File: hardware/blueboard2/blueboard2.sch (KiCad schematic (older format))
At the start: 142 parts, among them Q1 TRANSISTOR_NPN, Q2 TRANSISTOR_NPN, Q3 TRANSISTOR_NPN, SW2 SW_PUSHBUTTON

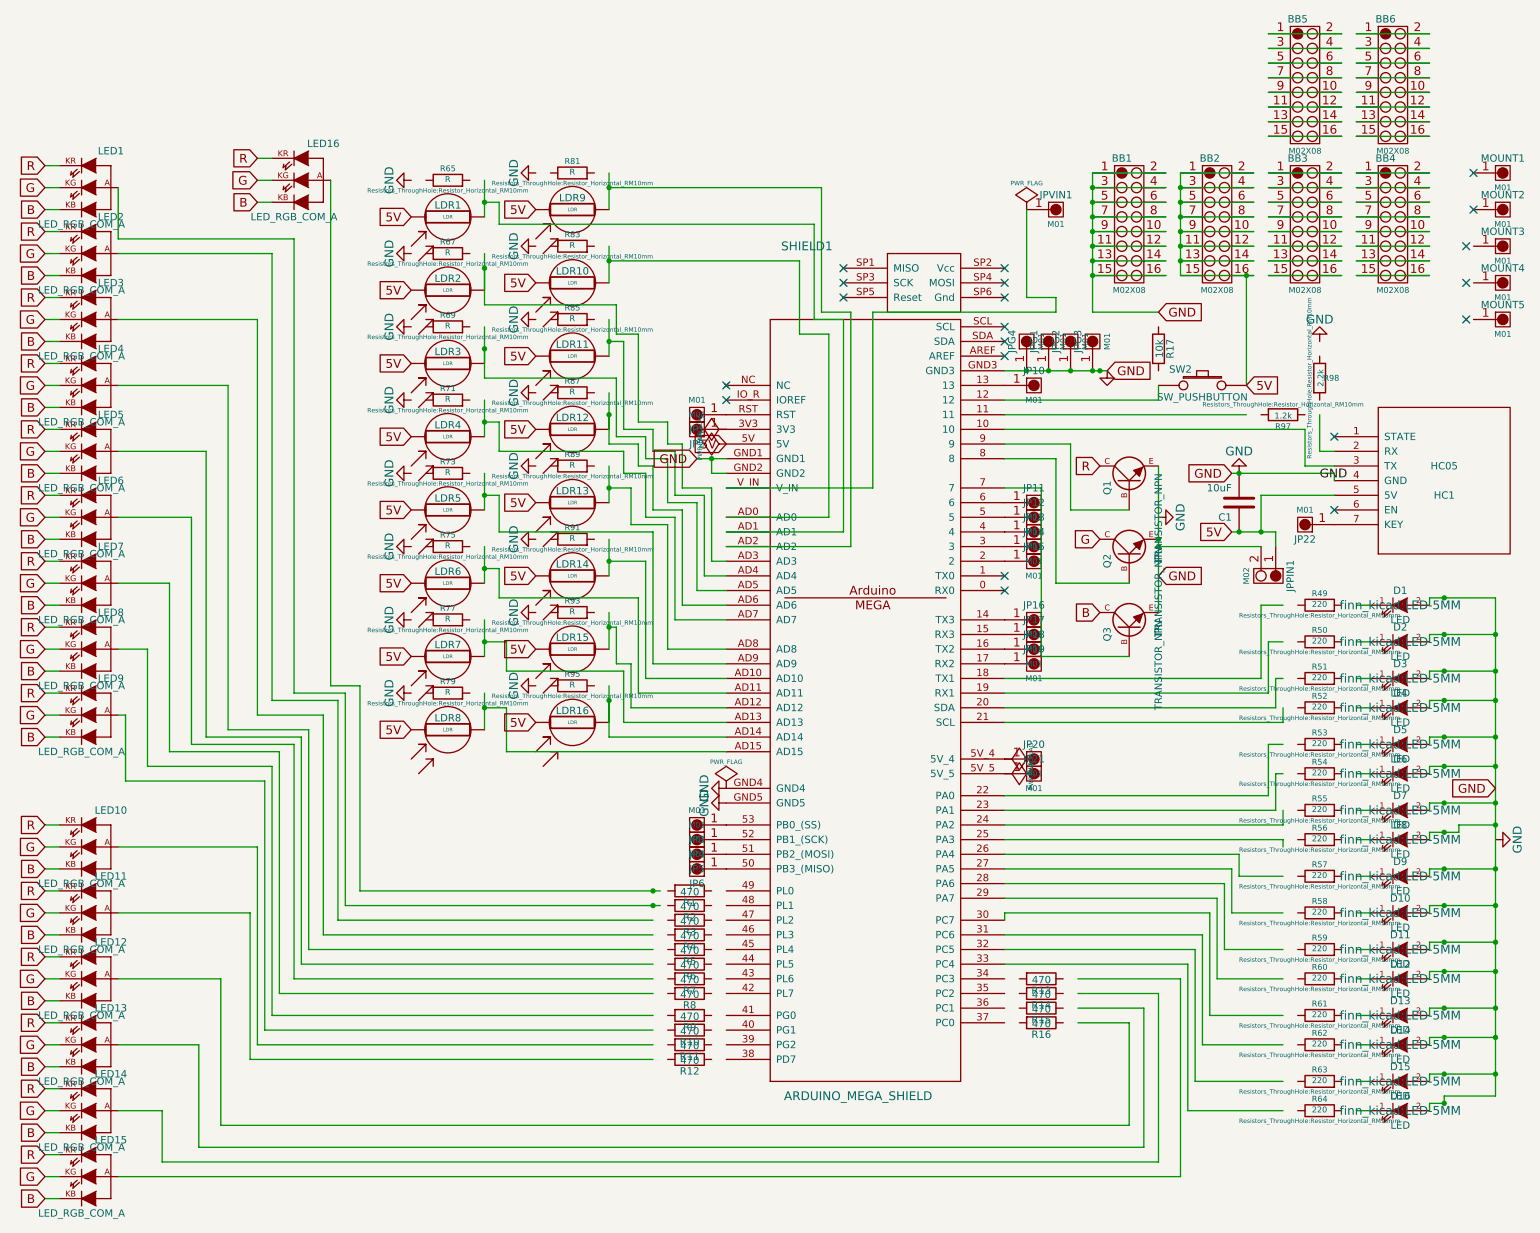
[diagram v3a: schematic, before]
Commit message: updated svgs to fit manufactured board. Reconnected resistors in schematica
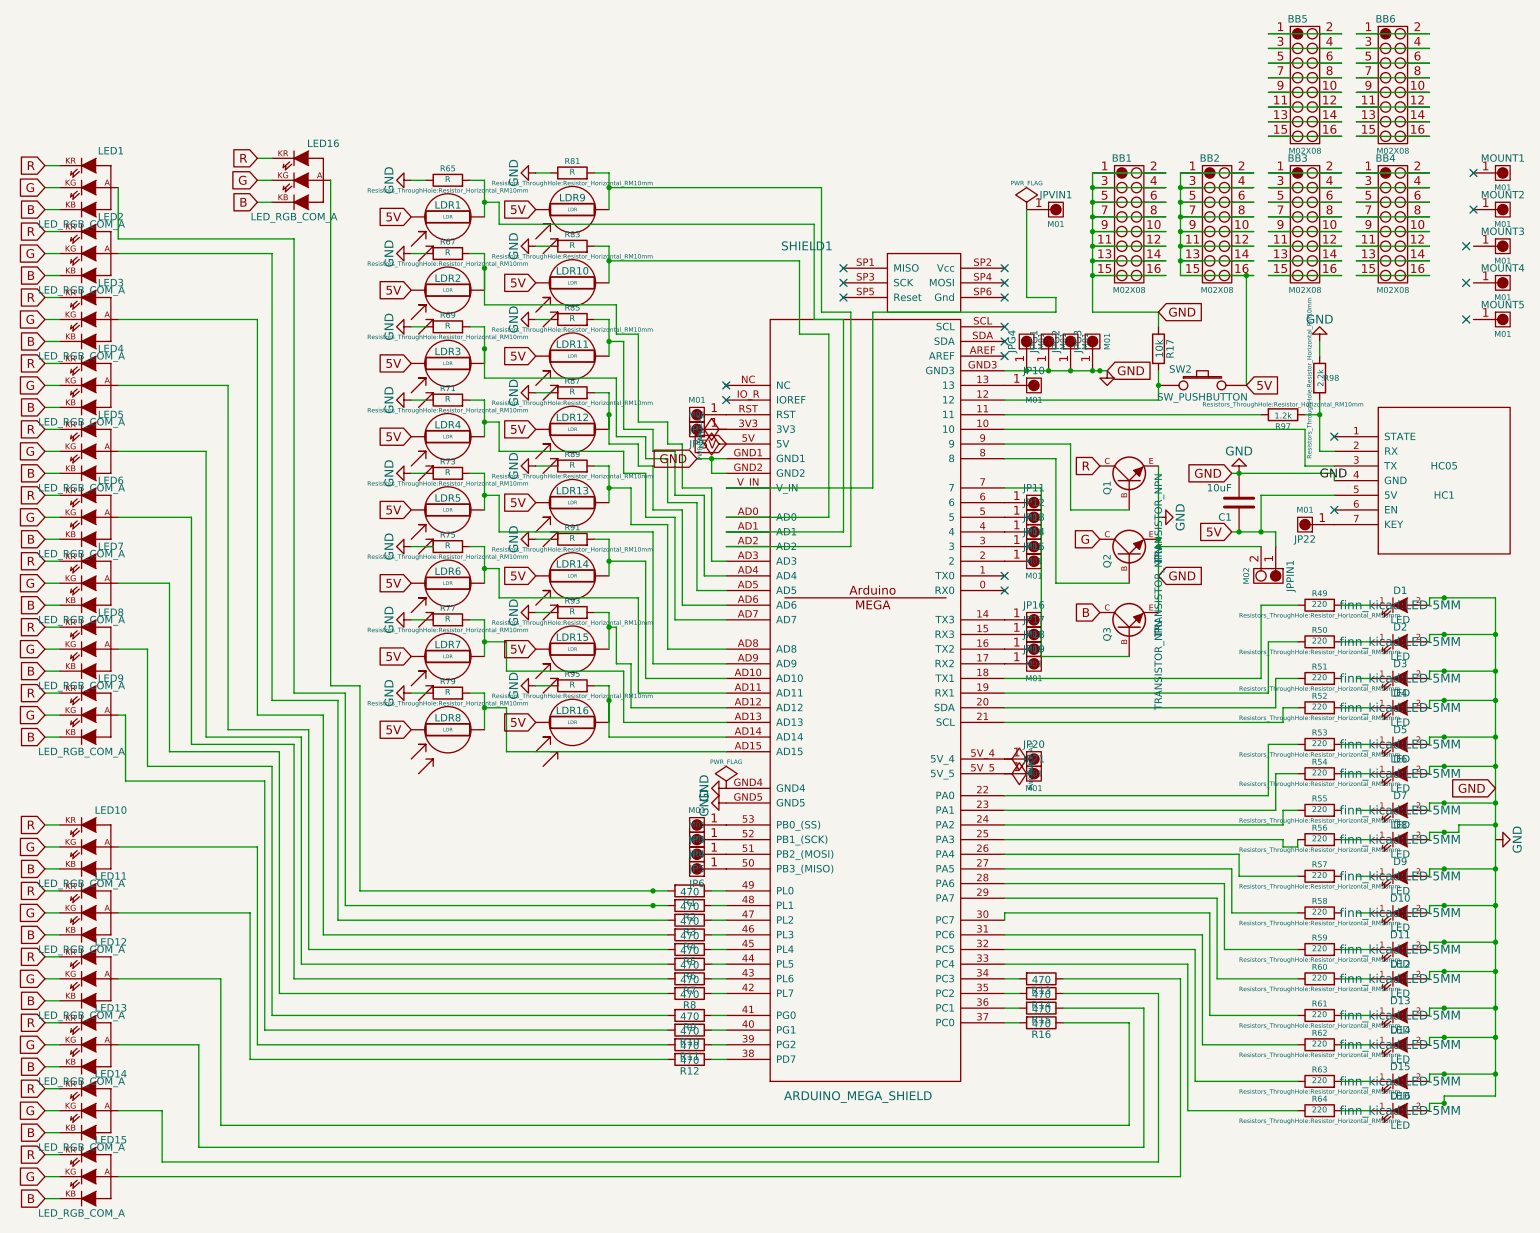
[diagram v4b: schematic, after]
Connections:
- wire segments 422 -> 477
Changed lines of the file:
@@
 	1700 5700 2600 5700
 Wire Wire Line
-	8600 7150 8600 6450
-Wire Wire Line
-	2400 7150 8600 7150
-Wire Wire Line
-	2400 6150 2400 7150
-Wire Wire Line
-	1700 6150 2400 6150
-Wire Wire Line
-	8700 7300 8700 6350
-Wire Wire Line
-	2250 7300 8700 7300
-Wire Wire Line
-	2250 6600 2250 7300
-Wire Wire Line
-	1700 6600 2250 6600
-Wire Wire Line
-	8800 7400 8800 6250
-Wire Wire Line
-	2000 7400 8800 7400
-Wire Wire Line
-	2000 7050 2000 7400
-Wire Wire Line
-	1700 7050 2000 7050
-Wire Wire Line
-	8950 7500 8950 6150
-Wire Wire Line
-	1700 7500 8950 7500
+	8600 6450 8600 7150
+Wire Wire Line
+	8600 7150 2400 7150
+Wire Wire Line
+	2400 7150 2400 6150
+Wire Wire Line
+	2400 6150 1700 6150
+Wire Wire Line
+	8700 6350 8700 7300
+Wire Wire Line
+	8700 7300 2250 7300
+Wire Wire Line
+	2250 7300 2250 6600
+Wire Wire Line
+	2250 6600 1700 6600
+Wire Wire Line
+	8800 6250 8800 7400
+Wire Wire Line
+	8800 7400 2000 7400
+Wire Wire Line
+	2000 7400 2000 7050
+Wire Wire Line
+	2000 7050 1700 7050
+Wire Wire Line
+	8950 6150 8950 7500
+Wire Wire Line
+	8950 7500 1700 7500
 Wire Wire Line
 	1300 1800 1200 1800
@@
 	10750 7000 10650 7000
 Wire Wire Line
-	10150 7050 10250 7050
+	10050 7050 10250 7050
 Wire Wire Line
 	10650 3550 10650 3600
@@
 	10650 3550 11100 3550
 Wire Wire Line
-	10150 3600 10250 3600
+	10050 3600 10250 3600
 Wire Wire Line
 	10650 6550 10650 6600
@@
 	11100 6550 10650 6550
 Wire Wire Line
-	10150 6600 10250 6600
+	10050 6600 10250 6600
 Wire Wire Line
 	10650 6800 10650 6850
@@
 	11100 6800 10650 6800
 Wire Wire Line
-	10150 6850 10250 6850
+	10050 6850 10250 6850
 Wire Wire Line
 	10650 6100 10650 6150
@@
 	11100 6100 10650 6100
 Wire Wire Line
-	10150 6150 10250 6150
+	10050 6150 10250 6150
 Wire Wire Line
 	10650 6350 10650 6400
@@
 	11100 6350 10650 6350
 Wire Wire Line
-	10150 6400 10250 6400
+	10050 6400 10250 6400
 Wire Wire Line
 	10650 5650 10650 5700
@@
 	11100 5900 10650 5900
 Wire Wire Line
-	10150 5950 10250 5950
+	10050 5950 10250 5950
 Wire Wire Line
 	10650 5150 10650 5200
@@
 	10650 5150 10850 5150
 Wire Wire Line
-	10150 5200 10250 5200
+	10050 5200 10250 5200
 Wire Wire Line
 	10650 5400 10650 5450
@@
 	11100 4700 10650 4700
 Wire Wire Line
-	10150 4750 10250 4750
+	10050 4750 10250 4750
 Wire Wire Line
 	10650 4950 10650 5000
@@
 	11100 4250 10650 4250
 Wire Wire Line
-	10150 4300 10250 4300
+	10050 4300 10250 4300
 Wire Wire Line
 	10650 4500 10650 4550
@@
 	11100 4500 10650 4500
 Wire Wire Line
-	10150 4550 10250 4550
+	10050 4550 10250 4550
 Wire Wire Line
 	10650 3800 10650 3850
@@
 	10650 3800 11100 3800
 Wire Wire Line
-	10150 3850 10250 3850
+	10050 3850 10250 3850
 Wire Wire Line
 	10650 4050 10650 4100
@@
 	9000 6050 9000 7050
 Wire Wire Line
-	9000 7050 9650 7050
+	9000 7050 9750 7050
 Wire Wire Line
 	9050 5950 9050 6850
 Wire Wire Line
-	9050 6850 9650 6850
+	9050 6850 9750 6850
 Wire Wire Line
 	9100 5850 9100 6600
 Wire Wire Line
-	9100 6600 9650 6600
+	9100 6600 9750 6600
 Wire Wire Line
 	9150 5700 9150 6400
 Wire Wire Line
-	9150 6400 9650 6400
+	9150 6400 9750 6400
 Wire Wire Line
 	9200 5600 9200 6150
 Wire Wire Line
-	9200 6150 9650 6150
+	9200 6150 9750 6150
 Wire Wire Line
 	9250 5500 9250 5950
 Wire Wire Line
-	9250 5950 9650 5950
+	9250 5950 9750 5950
 Wire Wire Line
 	9300 5400 9300 5700
 Wire Wire Line
-	9300 5700 9650 5700
+	9300 5700 9750 5700
 Wire Wire Line
 	9350 5300 9350 5450
 Wire Wire Line
-	9350 5450 9650 5450
+	9350 5450 9750 5450
 Wire Wire Line
 	9650 5100 9650 5000
@@
 	9600 5000 9600 4750
 Wire Wire Line
-	9600 4750 9650 4750
+	9600 4750 9750 4750
 Wire Wire Line
 	9550 4900 9550 4550
 Wire Wire Line
-	9550 4550 9650 4550
+	9550 4550 9750 4550
 Wire Wire Line
 	9650 4400 9650 4300
@@
 	9600 4300 9600 4100
 Wire Wire Line
-	9600 4100 9650 4100
+	9600 4100 9750 4100
 Wire Wire Line
 	9550 4200 9550 3850
 Wire Wire Line
-	9550 3850 9650 3850
+	9550 3850 9750 3850
 Wire Wire Line
 	9500 4100 9500 3600
 Wire Wire Line
-	9500 3600 9650 3600
+	9500 3600 9750 3600
 Text GLabel 9300 3100 0    60   Input ~ 0
 5V
@@
 $EndComp
 Wire Wire Line
-	7750 2300 9400 2300
+	7750 2300 9500 2300
 $Comp
 L R R98
@@
 $EndComp
 Wire Wire Line
-	3350 5550 5400 5550
+	3350 5550 5450 5550
 Connection ~ 5350 5550
 Wire Wire Line
-	3250 5650 5400 5650
+	3250 5650 5450 5650
 Connection ~ 5350 5650
 Wire Wire Line
-	3200 5750 5350 5750
-Wire Wire Line
-	3100 5850 5350 5850
-Wire Wire Line
-	3000 5950 5350 5950
-Wire Wire Line
-	2950 6050 5350 6050
-Wire Wire Line
-	2900 6150 5350 6150
-Wire Wire Line
-	2800 6250 5350 6250
-Wire Wire Line
-	2750 6400 5350 6400
-Wire Wire Line
-	2700 6500 5350 6500
-Wire Wire Line
-	2650 6600 5350 6600
-Wire Wire Line
-	2600 6700 5350 6700
+	3200 5750 5450 5750
+Wire Wire Line
+	3100 5850 5450 5850
+Wire Wire Line
+	3000 5950 5450 5950
+Wire Wire Line
+	2950 6050 5450 6050
+Wire Wire Line
+	2900 6150 5450 6150
+Wire Wire Line
+	2800 6250 5450 6250
+Wire Wire Line
+	2750 6400 5450 6400
+Wire Wire Line
+	2700 6500 5450 6500
+Wire Wire Line
+	2650 6600 5450 6600
+Wire Wire Line
+	2600 6700 5450 6700
 $Comp
 L R R16
@@
 $EndComp
 Wire Wire Line
-	8600 6450 8250 6450
-Wire Wire Line
-	8700 6350 8250 6350
-Wire Wire Line
-	8800 6250 8250 6250
-Wire Wire Line
-	8950 6150 8250 6150
+	8150 6450 8600 6450
+Wire Wire Line
+	8150 6350 8700 6350
+Wire Wire Line
+	8150 6250 8800 6250
+Wire Wire Line
+	8150 6150 8950 6150
 Wire Wire Line
 	9000 6050 7750 6050
@@
 $EndComp
 Wire Wire Line
-	10000 2550 9900 2550
-Wire Wire Line
-	9900 2550 9900 2300
+	9900 2550 10000 2550
+Wire Wire Line
+	9900 2200 9900 2550
 Wire Wire Line
 	9800 2400 9800 2650
@@
 $EndComp
 Wire Wire Line
-	7750 2200 8800 2200
-Wire Wire Line
-	8800 2200 8800 2100
+	8800 2200 7750 2200
+Wire Wire Line
+	8800 2000 8800 2200
 $Comp
 L R R17
@@
 	9600 3100 9600 3200
 Connection ~ 9500 3100
+Wire Wire Line
+	5750 5550 5850 5550
+Wire Wire Line
+	5850 5650 5750 5650
+Wire Wire Line
+	5850 5750 5750 5750
+Wire Wire Line
+	5850 5850 5750 5850
+Wire Wire Line
+	5850 5950 5750 5950
+Wire Wire Line
+	5850 6050 5750 6050
+Wire Wire Line
+	5850 6150 5750 6150
+Wire Wire Line
+	5850 6250 5750 6250
+Wire Wire Line
+	5850 6400 5750 6400
+Wire Wire Line
+	5850 6500 5750 6500
+Wire Wire Line
+	5850 6600 5750 6600
+Wire Wire Line
+	5850 6700 5750 6700
+Wire Wire Line
+	7750 6150 7850 6150
+Wire Wire Line
+	7750 6250 7850 6250
+Wire Wire Line
+	7750 6350 7850 6350
+Wire Wire Line
+	7750 6450 7850 6450
+Wire Wire Line
+	9650 4300 9750 4300
+Wire Wire Line
+	9650 5000 9750 5000
+Wire Wire Line
+	9650 5250 9750 5250
+Wire Wire Line
+	9750 5250 9750 5200
+Wire Wire Line
+	8800 1600 8800 1700
+Connection ~ 8800 2100
+Wire Wire Line
+	9900 1900 9900 1800
+Wire Wire Line
+	9900 2300 9800 2300
+Connection ~ 9900 2300
+Wire Wire Line
+	4200 700  4100 700
+Wire Wire Line
+	3800 700  3700 700
+Wire Wire Line
+	4200 1200 4100 1200
+Wire Wire Line
+	3800 1200 3700 1200
+Wire Wire Line
+	4200 1700 4100 1700
+Wire Wire Line
+	3800 1700 3700 1700
+Wire Wire Line
+	4200 2200 4100 2200
+Wire Wire Line
+	3800 2200 3700 2200
+Wire Wire Line
+	4200 2700 4100 2700
+Wire Wire Line
+	3800 2700 3700 2700
+Wire Wire Line
+	4200 3200 4100 3200
+Wire Wire Line
+	3850 3200 3700 3200
+Wire Wire Line
+	4200 3700 4100 3700
+Wire Wire Line
+	3800 3700 3700 3700
+Wire Wire Line
+	4200 4200 4100 4200
+Wire Wire Line
+	3800 4200 3700 4200
+Wire Wire Line
+	5050 4150 4950 4150
+Wire Wire Line
+	4650 4150 4550 4150
+Wire Wire Line
+	5050 3650 4950 3650
+Wire Wire Line
+	4650 3650 4550 3650
+Wire Wire Line
+	5050 3150 4950 3150
+Wire Wire Line
+	4650 3150 4550 3150
+Wire Wire Line
+	5050 2650 4950 2650
+Wire Wire Line
+	4650 2650 4550 2650
+Wire Wire Line
+	5050 2150 4950 2150
+Wire Wire Line
+	4650 2150 4550 2150
+Wire Wire Line
+	5050 1650 4950 1650
+Wire Wire Line
+	4650 1650 4550 1650
+Wire Wire Line
+	5050 1150 4950 1150
+Wire Wire Line
+	4650 1150 4550 1150
+Wire Wire Line
+	5050 650  4950 650
+Wire Wire Line
+	4650 650  4550 650
 $EndSCHEMATC
